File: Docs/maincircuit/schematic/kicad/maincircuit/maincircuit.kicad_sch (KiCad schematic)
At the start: 9 parts

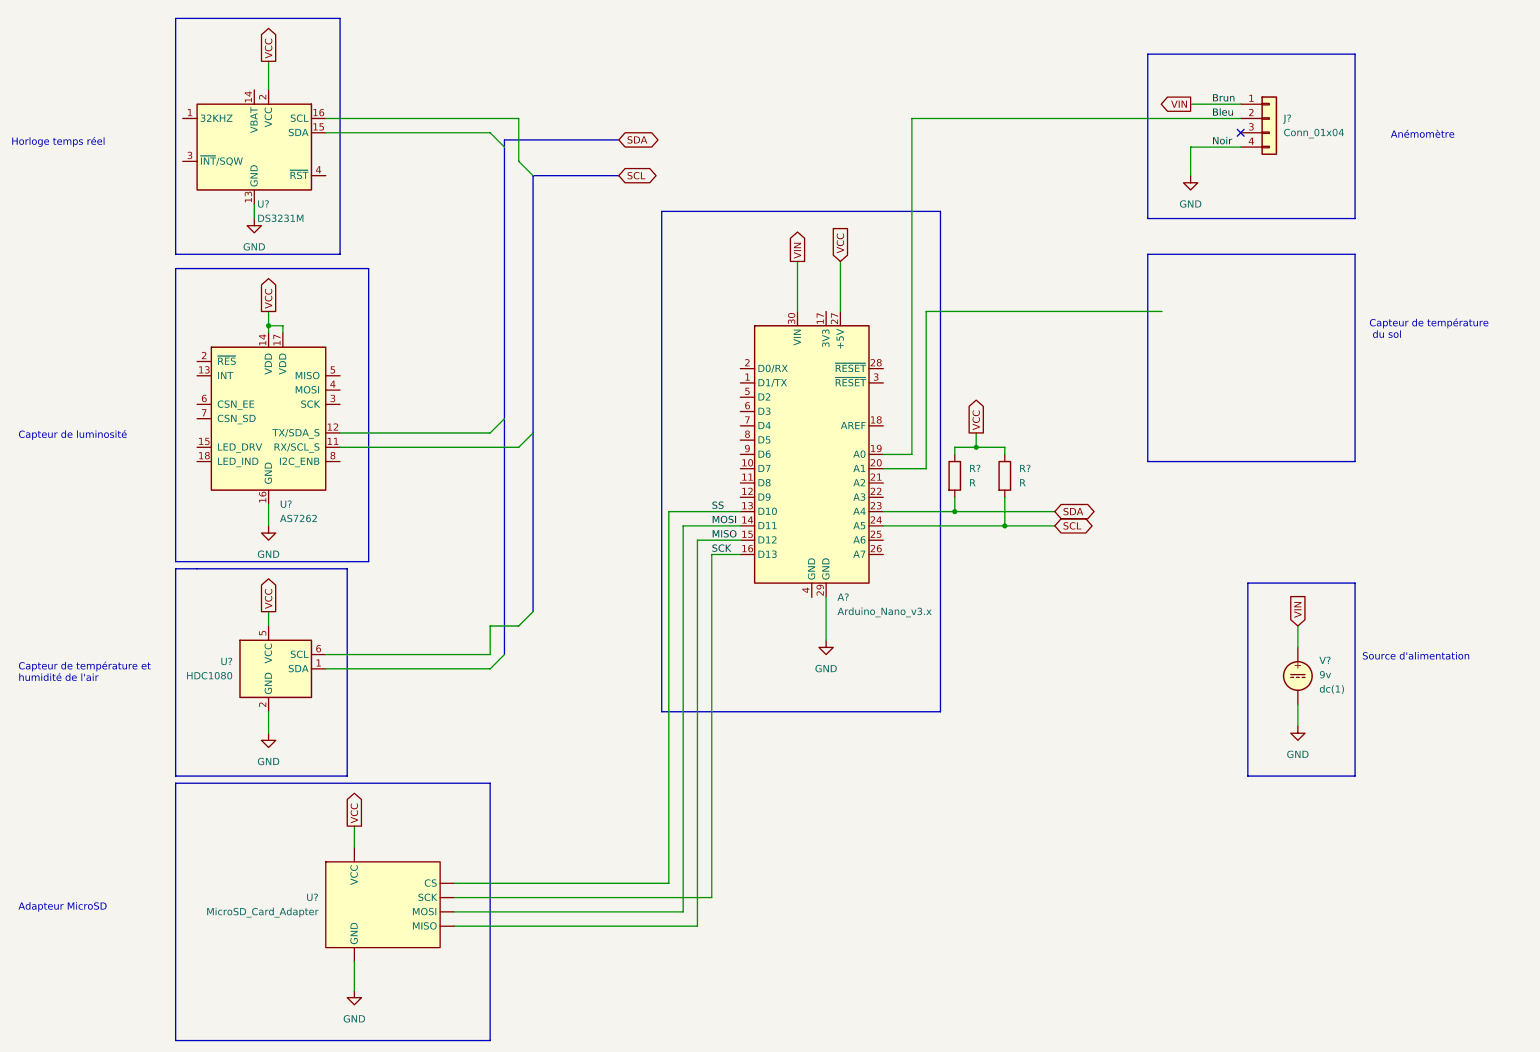
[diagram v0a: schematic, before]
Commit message: modif sd source 3V; enlever pullup ; revision 0.2
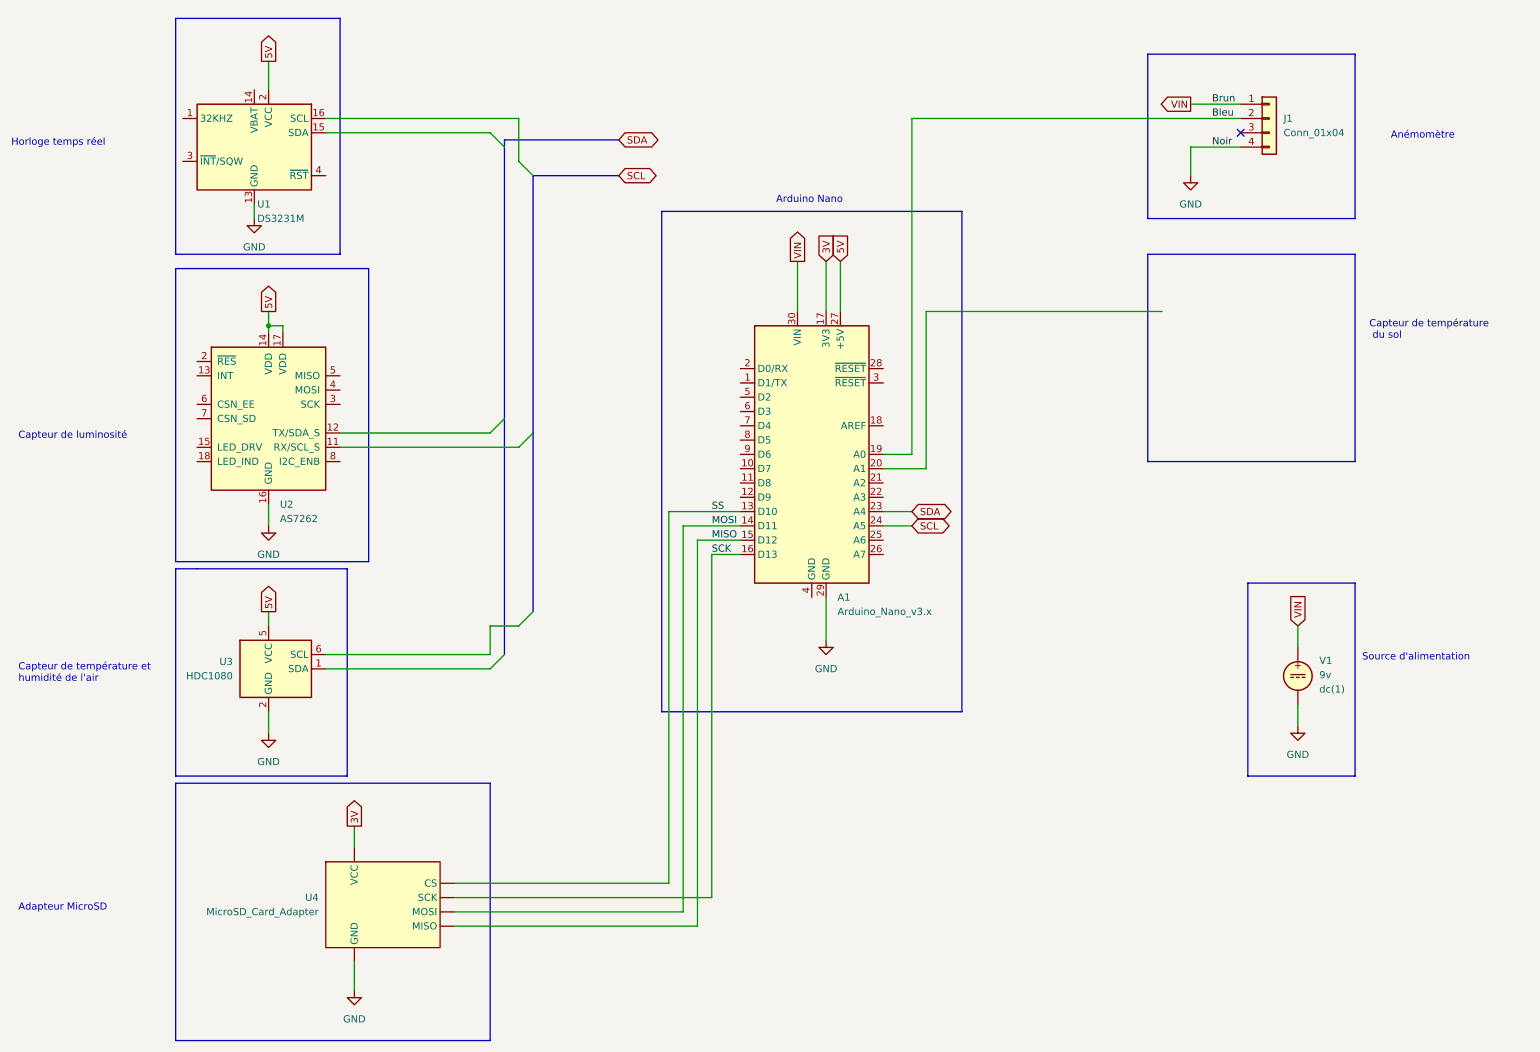
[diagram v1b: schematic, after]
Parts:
- removed R? (x2): R, symbol Device:R
- gave numbers to parts that had none: 7
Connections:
- net 3V: now reaches A1.17 (3V3)
- net 3V: now also U4. (VCC)
- net VCC renamed 5V
- net 5V: no longer U4. (VCC)
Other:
- note added: "Arduino Nano"

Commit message: mise a jours du diagramme de circuit - revision 1.0
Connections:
- net 5V: now also U4. (VCC)
- net Circuit_RTD_PT100/Sortie: now reaches A1.20 (A1)
- net 3V: no longer names the net of A1.17 (3V3)
- net 3V: no longer U4. (VCC)
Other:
- added sheet Circuit_RTD_PT100 (PFE_RTD.kicad_sch)
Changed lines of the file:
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@@
   (title_block
     (title "Station météo - Diagramme de circuit ")
-    (date "2022-03-29")
-    (rev "0.2")
+    (date "2022-04-05")
+    (rev "1.0")
     (company "ÉTS - PFE HIVER 2022 - ELE795")
     (comment 1 "NASRI, Mahan")
@@
     (stroke (width 0) (type default) (color 0 0 0 0))
   )
-  (wire (pts (xy 162.56 58.42) (xy 162.56 67.31))
-    (stroke (width 0) (type default) (color 0 0 0 0))
-  )
   (polyline (pts (xy 46.99 149.86) (xy 46.99 113.03))
     (stroke (width 0) (type default) (color 0 0 0 0))
@@
     (stroke (width 0) (type default) (color 0 0 0 0))
   )
-  (wire (pts (xy 180.34 67.31) (xy 222.25 67.31))
+  (wire (pts (xy 180.34 67.31) (xy 224.79 67.31))
     (stroke (width 0) (type default) (color 0 0 0 0))
   )
@@
     )
   )
-  (global_label "3V" (shape output) (at 78.74 158.75 90) (fields_autoplaced)
-    (effects (font (size 1.27 1.27)) (justify left))
-    (property "Intersheet References" "${INTERSHEET_REFS}" (id 0) (at 78.6606 154.0388 90)
-      (effects (font (size 1.27 1.27)) (justify left) hide)
-    )
-  )
   (global_label "SDA" (shape bidirectional) (at 177.8 102.87 0) (fields_autoplaced)
     (effects (font (size 1.27 1.27)) (justify left))
@@
     (effects (font (size 1.27 1.27)) (justify left))
     (property "Intersheet References" "${INTERSHEET_REFS}" (id 0) (at 165.0206 52.3783 90)
-      (effects (font (size 1.27 1.27)) (justify left) hide)
-    )
-  )
-  (global_label "3V" (shape input) (at 162.56 58.42 90) (fields_autoplaced)
-    (effects (font (size 1.27 1.27)) (justify left))
-    (property "Intersheet References" "${INTERSHEET_REFS}" (id 0) (at 162.4806 53.7088 90)
       (effects (font (size 1.27 1.27)) (justify left) hide)
     )
@@
     (effects (font (size 1.27 1.27)) (justify left))
     (property "Intersheet References" "${INTERSHEET_REFS}" (id 0) (at 131.6507 43.1006 0)
+      (effects (font (size 1.27 1.27)) (justify left) hide)
+    )
+  )
+  (global_label "5V" (shape output) (at 78.74 158.75 90) (fields_autoplaced)
+    (effects (font (size 1.27 1.27)) (justify left))
+    (property "Intersheet References" "${INTERSHEET_REFS}" (id 0) (at 78.6606 152.7083 90)
       (effects (font (size 1.27 1.27)) (justify left) hide)
     )
@@
     (pin "1")
   )
+  (sheet (at 224.79 60.96) (size 26.67 27.94) (fields_autoplaced)
+    (stroke (width 0.1524) (type solid) (color 0 0 0 0))
+    (fill (color 0 0 0 0.0000))
+    (property "Sheet name" "Circuit_RTD_PT100" (id 0) (at 224.79 60.2484 0)
+      (effects (font (size 1.27 1.27)) (justify left bottom))
+    )
+    (property "Sheet file" "PFE_RTD.kicad_sch" (id 1) (at 224.79 89.4846 0)
+      (effects (font (size 1.27 1.27)) (justify left top))
+    )
+    (pin "Sortie" output (at 224.79 67.31 180)
+      (effects (font (size 1.27 1.27)) (justify left))
+    )
+  )
   (sheet_instances
     (path "/" (page "1"))
+    (path "/806a040a-651b-439f-9240-0e13101ec59b" (page "2"))
   )
   (symbol_instances
@@
       (reference "#PWR07") (unit 1) (value "GND") (footprint "")
     )
+    (path "/806a040a-651b-439f-9240-0e13101ec59b/2ed77dab-9d3c-4561-bfa6-92dc6a7e27b7"
+      (reference "#PWR08") (unit 1) (value "GND") (footprint "")
+    )
+    (path "/806a040a-651b-439f-9240-0e13101ec59b/7f89682d-1838-422d-b1f3-eeaa3bc004ff"
+      (reference "#PWR09") (unit 1) (value "GND") (footprint "")
+    )
+    (path "/806a040a-651b-439f-9240-0e13101ec59b/cf772c03-fb44-49da-879b-fbf9668d529b"
+      (reference "#PWR010") (unit 1) (value "GND") (footprint "")
+    )
+    (path "/806a040a-651b-439f-9240-0e13101ec59b/bc6c0cfa-87ac-4a1b-87e3-eac3144ed737"
+      (reference "#PWR011") (unit 1) (value "GND") (footprint "")
+    )
+    (path "/806a040a-651b-439f-9240-0e13101ec59b/501193c8-4eda-4951-b814-14b4cf9d4de2"
+      (reference "#PWR012") (unit 1) (value "GND") (footprint "")
+    )
     (path "/136f24ab-7b8a-4b96-87e9-b51854289072"
       (reference "A1") (unit 1) (value "Arduino_Nano_v3.x") (footprint "Module:Arduino_Nano")
@@
       (reference "J1") (unit 1) (value "Conn_01x04") (footprint "")
     )
+    (path "/806a040a-651b-439f-9240-0e13101ec59b/ad2404c6-4ebc-4c59-b4a0-c769f8c853bf"
+      (reference "R1") (unit 1) (value "2.2k") (footprint "")
+    )
+    (path "/806a040a-651b-439f-9240-0e13101ec59b/accebe4a-4811-45d8-8b08-88051390a08a"
+      (reference "R2") (unit 1) (value "68") (footprint "")
+    )
+    (path "/806a040a-651b-439f-9240-0e13101ec59b/db4f3c25-f8e7-4f26-99f8-988930ae814e"
+      (reference "R3") (unit 1) (value "2.2k") (footprint "")
+    )
+    (path "/806a040a-651b-439f-9240-0e13101ec59b/8e8991b4-e67e-41ed-84b1-ecd433d4e14f"
+      (reference "R4") (unit 1) (value "1k") (footprint "")
+    )
+    (path "/806a040a-651b-439f-9240-0e13101ec59b/47f67289-7364-45d4-885b-8f979b51f8cd"
+      (reference "R5") (unit 1) (value "1k") (footprint "")
+    )
+    (path "/806a040a-651b-439f-9240-0e13101ec59b/da65892e-d331-4b58-b238-fc5e3ae49daf"
+      (reference "R6") (unit 1) (value "39k") (footprint "")
+    )
+    (path "/806a040a-651b-439f-9240-0e13101ec59b/32aa336b-a858-47f4-b2ce-a661ec9ff34b"
+      (reference "R7") (unit 1) (value "39k") (footprint "")
+    )
+    (path "/806a040a-651b-439f-9240-0e13101ec59b/fef95238-d472-4d2e-a0c1-16789adce777"
+      (reference "TH1") (unit 1) (value "PT100") (footprint "")
+    )
     (path "/361247c4-b43c-47ef-b3c8-f8ff60f69348"
       (reference "U1") (unit 1) (value "DS3231M") (footprint "Package_SO:SOIC-16W_7.5x10.3mm_P1.27mm")
@@
       (reference "U4") (unit 1) (value "MicroSD_Card_Adapter") (footprint "")
     )
+    (path "/806a040a-651b-439f-9240-0e13101ec59b/7122a679-0d1d-4bc8-a92d-965bd8303494"
+      (reference "U5") (unit 1) (value "MCP6042") (footprint "")
+    )
+    (path "/806a040a-651b-439f-9240-0e13101ec59b/47ea8403-309f-4b8a-bc8b-bf702d94c456"
+      (reference "U6") (unit 1) (value "MCP6042") (footprint "")
+    )
+    (path "/806a040a-651b-439f-9240-0e13101ec59b/b7333a97-7cde-42ee-afa0-6bd98eded848"
+      (reference "U7") (unit 1) (value "MCP6042") (footprint "")
+    )
     (path "/8e606922-08c7-4d14-8e6b-d1873e169fc8"

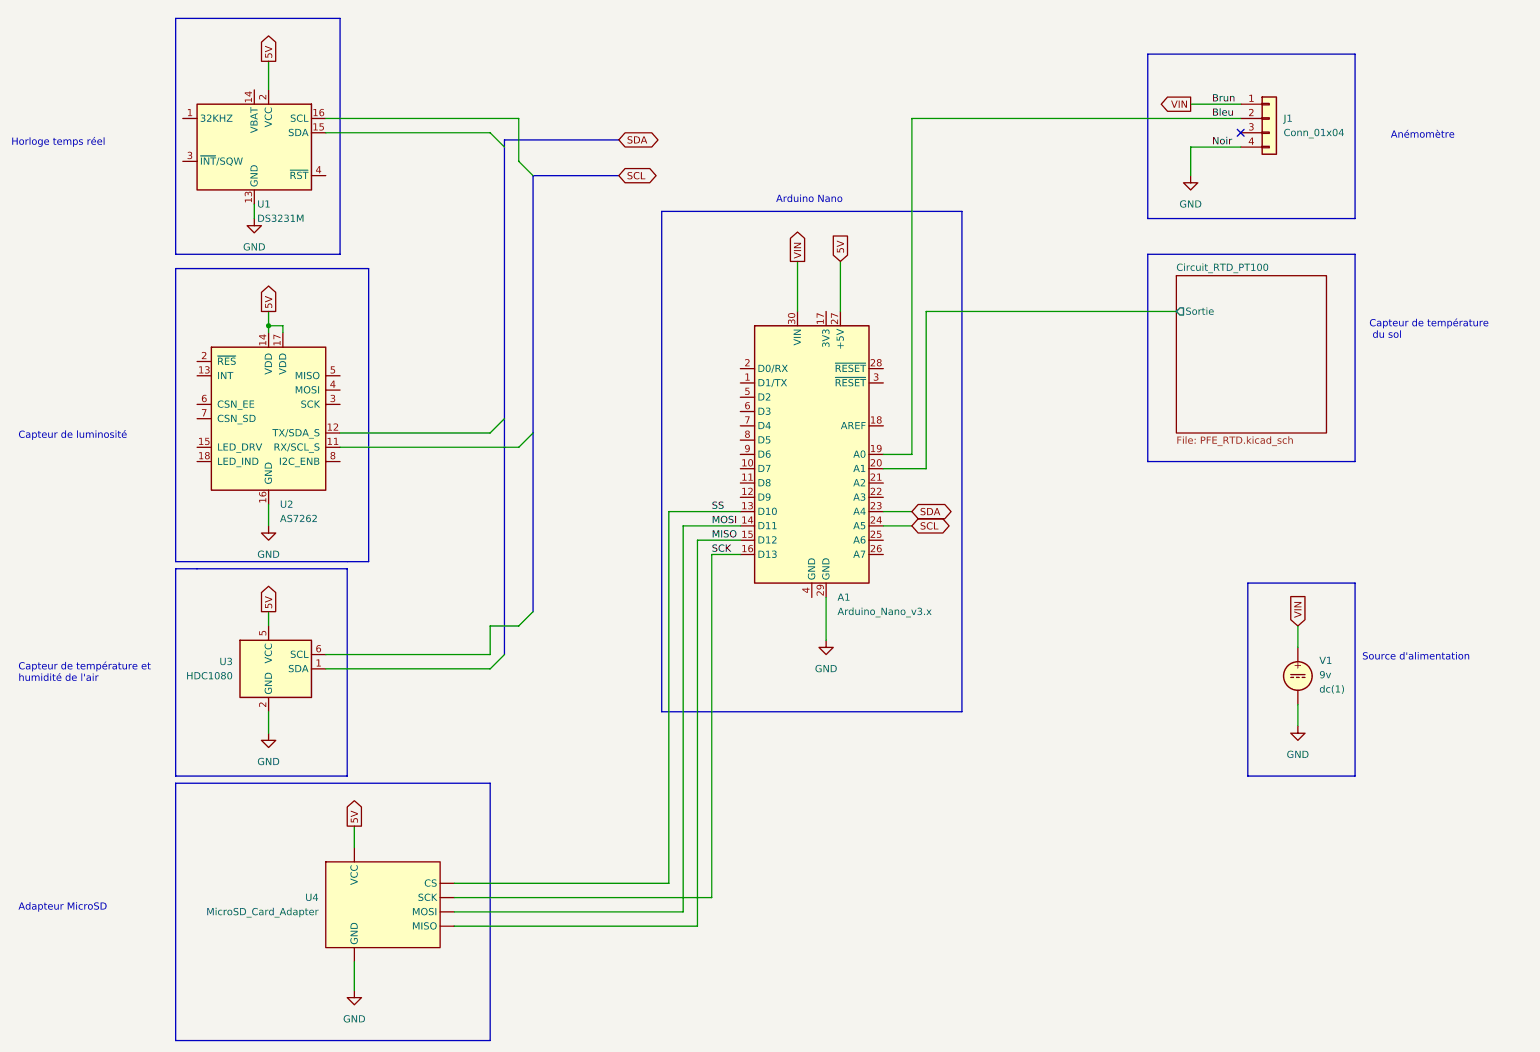
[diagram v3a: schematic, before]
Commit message: diagramme de circuit version 1.2 : ajout du circuit de relais + modif
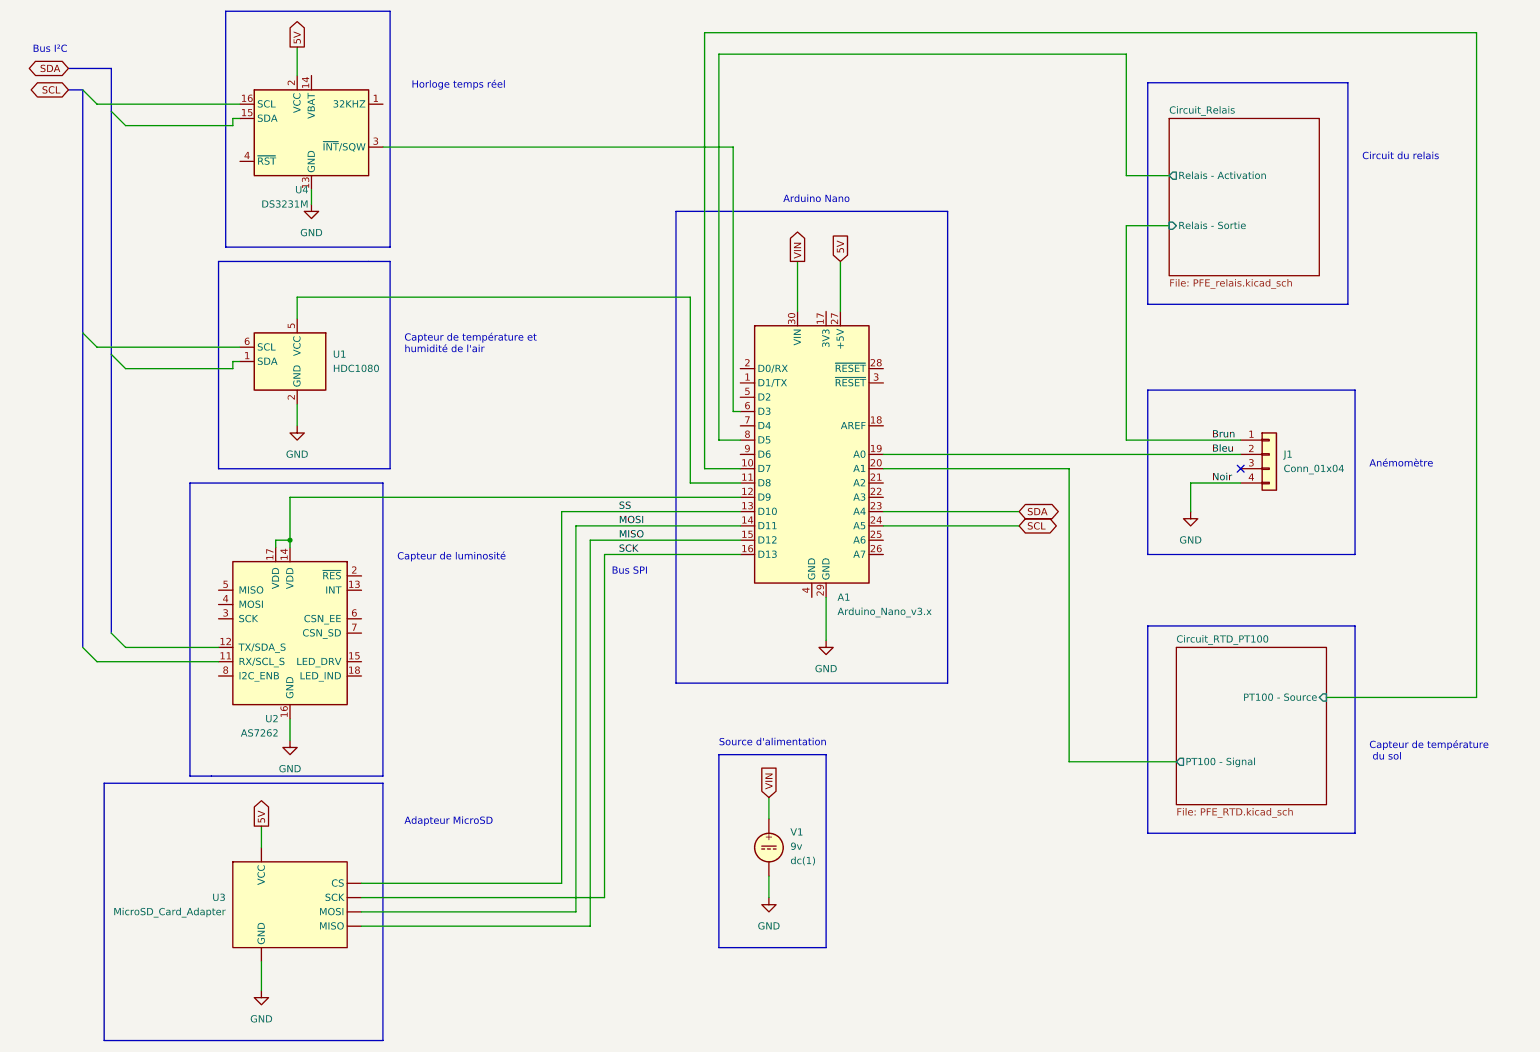
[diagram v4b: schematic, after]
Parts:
- renumbered U3 to U1, U4 to U3, U1 to U4
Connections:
- net 5V: no longer U1.5 (VCC), U2.14 (VDD), U2.17 (VDD)
- net VIN: no longer J1.1 (Pin_1)
- net Circuit_RTD_PT100/PT100 - Source: now reaches A1.10 (D7)
- net at A1.11 (D8): now also U1.5 (VCC)
- net at A1.12 (D9): now also U2.14 (VDD), U2.17 (VDD)
- net at A1.6 (D3): now also U4.3 (~{INT}/SQW)
- net Circuit_Relais/Relais - Activation: now reaches A1.8 (D5)
- net Circuit_RTD_PT100/Sortie renamed Circuit_RTD_PT100/PT100 - Signal
- new net Brun: J1.1 (Pin_1)
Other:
- added sheet Circuit_Relais (PFE_relais.kicad_sch)
- sheet Circuit_RTD_PT100 ports: added PT100 - Signal, PT100 - Source; removed Sortie
- note added: "Bus I²C"
- note added: "Bus SPI"
- note added: "Circuit du relais"
- moved on the sheet: J1, U1, U2, U3, U4, V1
